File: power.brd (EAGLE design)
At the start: 65 x 80 mm, 19 parts, among them J1 Battery, J2 Solar, J3 Battery

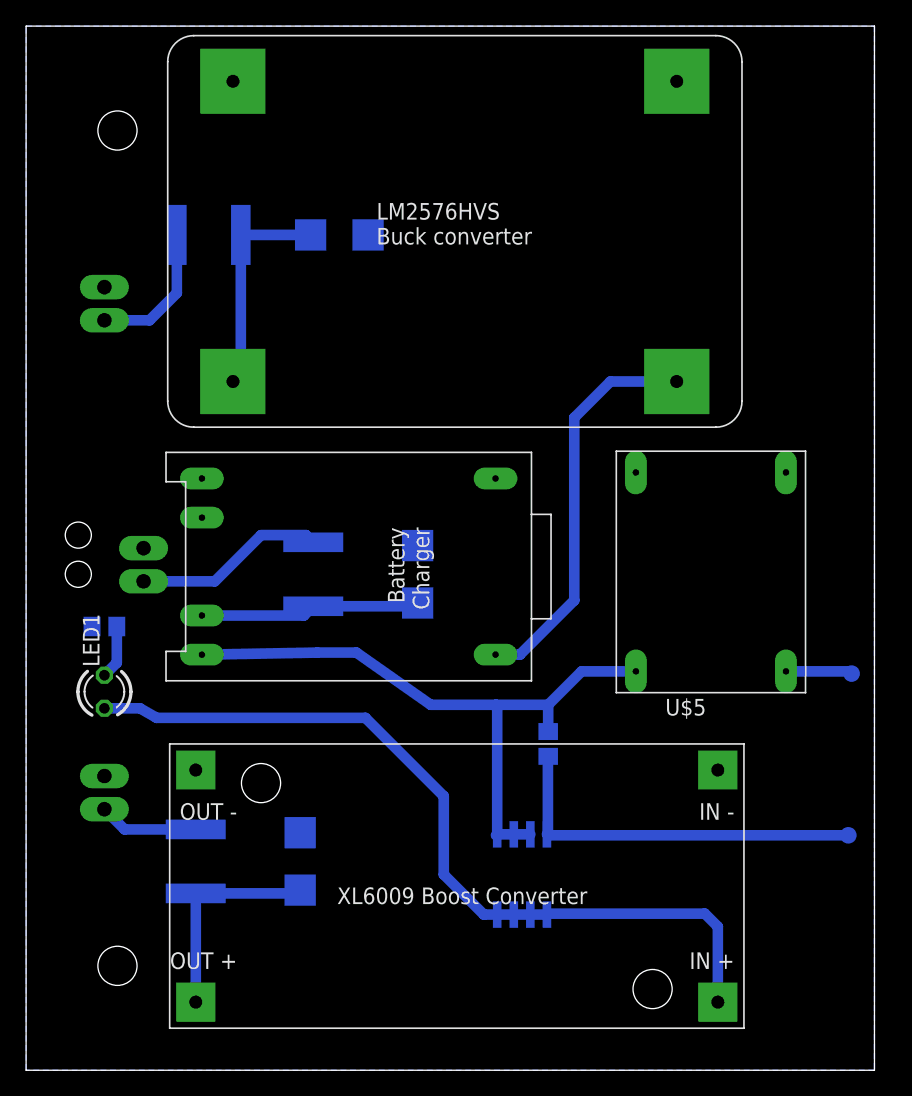
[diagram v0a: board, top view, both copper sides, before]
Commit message: Reworked power board
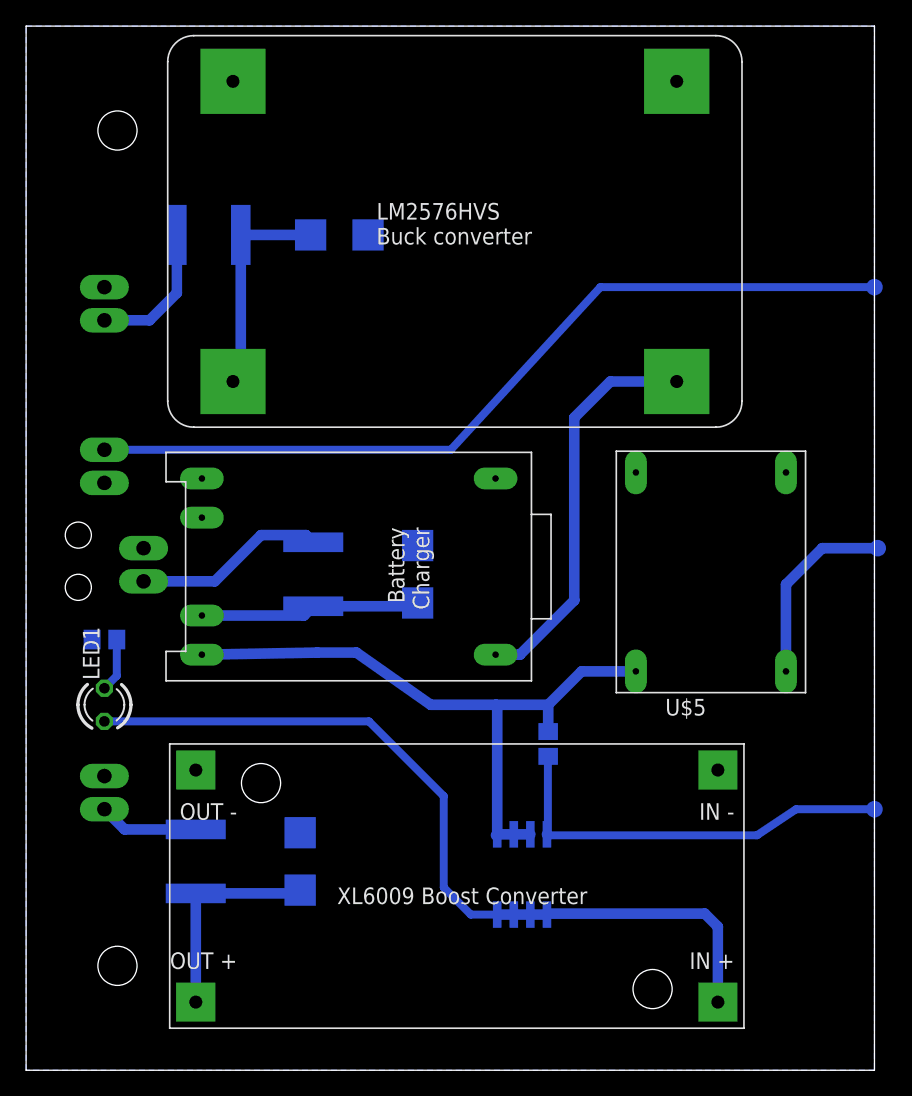
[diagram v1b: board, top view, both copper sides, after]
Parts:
- added J4: Button, SparkFun-Connectors:1X02_LONGPADS
- added TP1: TPSB1,27, testpad:B1,27
- J3: value Battery -> Valve
- U$3: value 2A -> 1A
- moved TP3 9.82 mm to (65.2, 40.0)
- moved TP5 2.83 mm to (65.0, 20.0)
- moved LED1 1.00 mm to (6.00, 28.0)
- moved R3 1.00 mm to (6.00, 33.0)
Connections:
- new net BUTTON_WAKEUP_INT: J4.2, TP1.TP
- net GND: now also J4.1
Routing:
- net BUTTON_WAKEUP_INT: track 0.00 -> 64.5 mm
- net VCC5: track 5.10 -> 14.8 mm
- net BT_POWER_ENABLE: track 29.2 -> 31.8 mm
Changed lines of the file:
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@@
 <hole x="7" y="8" drill="3"/>
 <hole x="4" y="41" drill="2"/>
-<hole x="4" y="38" drill="2"/>
+<hole x="4" y="37" drill="2"/>
 </plain>
 <attributes>
@@
 <element name="J1" library="SparkFun-Connectors" package="1X02_LONGPADS" value="Battery" x="9" y="40" rot="R270"/>
 <element name="J2" library="SparkFun-Connectors" package="1X02_LONGPADS" value="Solar" x="6" y="60" rot="R270"/>
-<element name="TP3" library="testpad" library_urn="urn:adsk.eagle:library:385" package="B1,27" package3d_urn="urn:adsk.eagle:package:27944/1" value="TPSB1,27" x="63.25" y="30.39" rot="MR0">
-<attribute name="TP_SIGNAL_NAME" value="" x="63.25" y="30.39" size="1.778" layer="28" rot="MR0" display="off"/>
+<element name="TP3" library="testpad" library_urn="urn:adsk.eagle:library:385" package="B1,27" package3d_urn="urn:adsk.eagle:package:27944/1" value="TPSB1,27" x="65.25" y="40" rot="MR0">
+<attribute name="TP_SIGNAL_NAME" value="" x="65.25" y="40" size="1.778" layer="28" rot="MR0" display="off"/>
 </element>
 <element name="U$10" library="fuse" library_urn="urn:adsk.eagle:library:233" package="MF-SMDF050" package3d_urn="urn:adsk.eagle:package:14081/1" value="500mA" x="14" y="64" rot="MR180"/>
@@
 <element name="U$5" library="breakout-modules" package="QSKJ_BOOST_MODULE" value="QSKJ_BOOST_MODULE" x="52.47" y="38.18"/>
 <element name="U$8" library="breakout-modules" package="LM2576HVS_BUCK_MODULE" value="LM2576HVS_BUCK_MODULE" x="10.85" y="49.27"/>
-<element name="LED1" library="led" library_urn="urn:adsk.eagle:library:259" package="LED3MM" package3d_urn="urn:adsk.eagle:package:15797/1" value="GREEN" x="6" y="29" rot="R90"/>
-<element name="R3" library="resistor" library_urn="urn:adsk.eagle:library:348" package="R0805" package3d_urn="urn:adsk.eagle:package:26059/1" value="3K3" x="6" y="34" rot="MR0"/>
+<element name="LED1" library="led" library_urn="urn:adsk.eagle:library:259" package="LED3MM" package3d_urn="urn:adsk.eagle:package:15797/1" value="GREEN" x="6" y="28" rot="R90"/>
+<element name="R3" library="resistor" library_urn="urn:adsk.eagle:library:348" package="R0805" package3d_urn="urn:adsk.eagle:package:26059/1" value="3K3" x="6" y="33" rot="MR0"/>
 <element name="R1" library="resistor" library_urn="urn:adsk.eagle:library:348" package="R0805" package3d_urn="urn:adsk.eagle:package:26059/1" value="1M" x="40" y="25" rot="MR270"/>
 <element name="U$6" library="breakout-modules" package="XL6009_BOOST_MODULE" value="XL6009_BOOST_MODULE" x="53" y="23" rot="R180"/>
 <element name="U$9" library="Semiconductors" package="SO08" value="FDS6675" x="38" y="15" rot="MR180"/>
-<element name="U$3" library="fuse" library_urn="urn:adsk.eagle:library:233" package="MF-SMDF050" package3d_urn="urn:adsk.eagle:package:14081/1" value="2A" x="13" y="16" rot="MR90"/>
+<element name="U$3" library="fuse" library_urn="urn:adsk.eagle:library:233" package="MF-SMDF050" package3d_urn="urn:adsk.eagle:package:14081/1" value="1A" x="13" y="16" rot="MR90"/>
 <element name="D4" library="diode" library_urn="urn:adsk.eagle:library:210" package="SMB" package3d_urn="urn:adsk.eagle:package:43404/2" value="" x="21" y="16" rot="MR90"/>
-<element name="J3" library="SparkFun-Connectors" package="1X02_LONGPADS" value="Battery" x="6" y="20" rot="R90"/>
-<element name="TP5" library="testpad" library_urn="urn:adsk.eagle:library:385" package="B1,27" package3d_urn="urn:adsk.eagle:package:27944/1" value="TPSB1,27" x="63" y="18" rot="MR0">
-<attribute name="TP_SIGNAL_NAME" value="" x="63" y="18" size="1.778" layer="28" rot="MR0" display="off"/>
+<element name="J3" library="SparkFun-Connectors" package="1X02_LONGPADS" value="Valve" x="6" y="20" rot="R90"/>
+<element name="TP5" library="testpad" library_urn="urn:adsk.eagle:library:385" package="B1,27" package3d_urn="urn:adsk.eagle:package:27944/1" value="TPSB1,27" x="65" y="20" rot="MR0">
+<attribute name="TP_SIGNAL_NAME" value="" x="65" y="20" size="1.778" layer="28" rot="MR0" display="off"/>
+</element>
+<element name="J4" library="SparkFun-Connectors" package="1X02_LONGPADS" value="Button" x="6" y="45" rot="R90"/>
+<element name="TP1" library="testpad" library_urn="urn:adsk.eagle:library:385" package="B1,27" package3d_urn="urn:adsk.eagle:package:27944/1" value="TPSB1,27" x="65" y="60" rot="MR90">
+<attribute name="TP_SIGNAL_NAME" value="" x="65" y="60" size="1.778" layer="28" rot="MR90" display="off"/>
 </element>
 </elements>
@@
 <contactref element="D4" pad="A"/>
 <contactref element="J3" pad="2"/>
+<contactref element="J4" pad="1"/>
 </signal>
 <signal name="VCC5">
 <contactref element="U$5" pad="V_OUT"/>
 <contactref element="TP3" pad="TP"/>
-<wire x1="58.22" y1="30.56" x2="63.08" y2="30.56" width="0.8128" layer="16"/>
-<wire x1="63.08" y1="30.56" x2="63.25" y2="30.39" width="0.8128" layer="16"/>
+<wire x1="58.22" y1="30.56" x2="58.22" y2="37.22" width="0.8128" layer="16"/>
+<wire x1="58.22" y1="37.22" x2="61" y2="40" width="0.8128" layer="16"/>
+<wire x1="61" y1="40" x2="65.25" y2="40" width="0.8128" layer="16"/>
 </signal>
 <signal name="V_CHARGER">
@@
 <contactref element="R3" pad="1"/>
 <contactref element="LED1" pad="K"/>
-<wire x1="6.95" y1="34" x2="6.95" y2="31.22" width="0.8128" layer="16"/>
-<wire x1="6.95" y1="31.22" x2="6" y2="30.27" width="0.8128" layer="16"/>
+<wire x1="6" y1="29.27" x2="6.95" y2="30.22" width="0.6096" layer="16"/>
+<wire x1="6.95" y1="30.22" x2="6.95" y2="33" width="0.6096" layer="16"/>
 </signal>
 <signal name="BT_POWER_ENABLE">
@@
 <contactref element="TP5" pad="TP"/>
 <wire x1="39.905" y1="18.0734" x2="39.9784" y2="18" width="0.8128" layer="16"/>
-<wire x1="39.9784" y1="18" x2="63" y2="18" width="0.8128" layer="16"/>
+<wire x1="39.9784" y1="18" x2="56" y2="18" width="0.6096" layer="16"/>
+<wire x1="56" y1="18" x2="59" y2="20" width="0.6096" layer="16"/>
+<wire x1="59" y1="20" x2="65" y2="20" width="0.6096" layer="16"/>
 <wire x1="40" y1="24.05" x2="39.9784" y2="24.0284" width="0.8128" layer="16"/>
-<wire x1="39.9784" y1="24.0284" x2="39.9784" y2="18" width="0.8128" layer="16"/>
+<wire x1="39.9784" y1="24.0284" x2="39.9784" y2="18" width="0.6096" layer="16"/>
 </signal>
 <signal name="V_VALVE_UNREG">
@@
 <wire x1="39.905" y1="11.9266" x2="39.9784" y2="12" width="0.8128" layer="16"/>
 <wire x1="39.9784" y1="12" x2="52" y2="12" width="0.8128" layer="16"/>
-<wire x1="26" y1="27" x2="10" y2="27" width="0.8128" layer="16"/>
-<wire x1="26" y1="27" x2="32" y2="21" width="0.8128" layer="16"/>
-<wire x1="32" y1="21" x2="32" y2="15" width="0.8128" layer="16"/>
-<wire x1="32" y1="15" x2="35.0734" y2="11.9266" width="0.8128" layer="16"/>
-<wire x1="35.0734" y1="11.9266" x2="36.095" y2="11.9266" width="0.8128" layer="16"/>
-<wire x1="10" y1="27" x2="8.73" y2="27.73" width="0.8128" layer="16"/>
-<wire x1="8.73" y1="27.73" x2="6" y2="27.73" width="0.8128" layer="16"/>
+<wire x1="6" y1="26.73" x2="26.27" y2="26.73" width="0.6096" layer="16"/>
+<wire x1="26.27" y1="26.73" x2="32" y2="21" width="0.6096" layer="16"/>
+<wire x1="32" y1="21" x2="32" y2="14" width="0.6096" layer="16"/>
+<wire x1="32" y1="14" x2="34.0734" y2="11.9266" width="0.6096" layer="16"/>
+<wire x1="34.0734" y1="11.9266" x2="36.095" y2="11.9266" width="0.6096" layer="16"/>
 </signal>
 <signal name="VALVE">
@@
 <wire x1="20.75" y1="13.55" x2="21" y2="13.8" width="0.8128" layer="16"/>
 </signal>
+<signal name="BUTTON_WAKEUP_INT">
+<contactref element="TP1" pad="TP"/>
+<contactref element="J4" pad="2"/>
+<wire x1="6" y1="47.54" x2="32.54" y2="47.54" width="0.6096" layer="16"/>
+<wire x1="32.54" y1="47.54" x2="44" y2="60" width="0.6096" layer="16"/>
+<wire x1="44" y1="60" x2="65" y2="60" width="0.6096" layer="16"/>
+</signal>
 </signals>

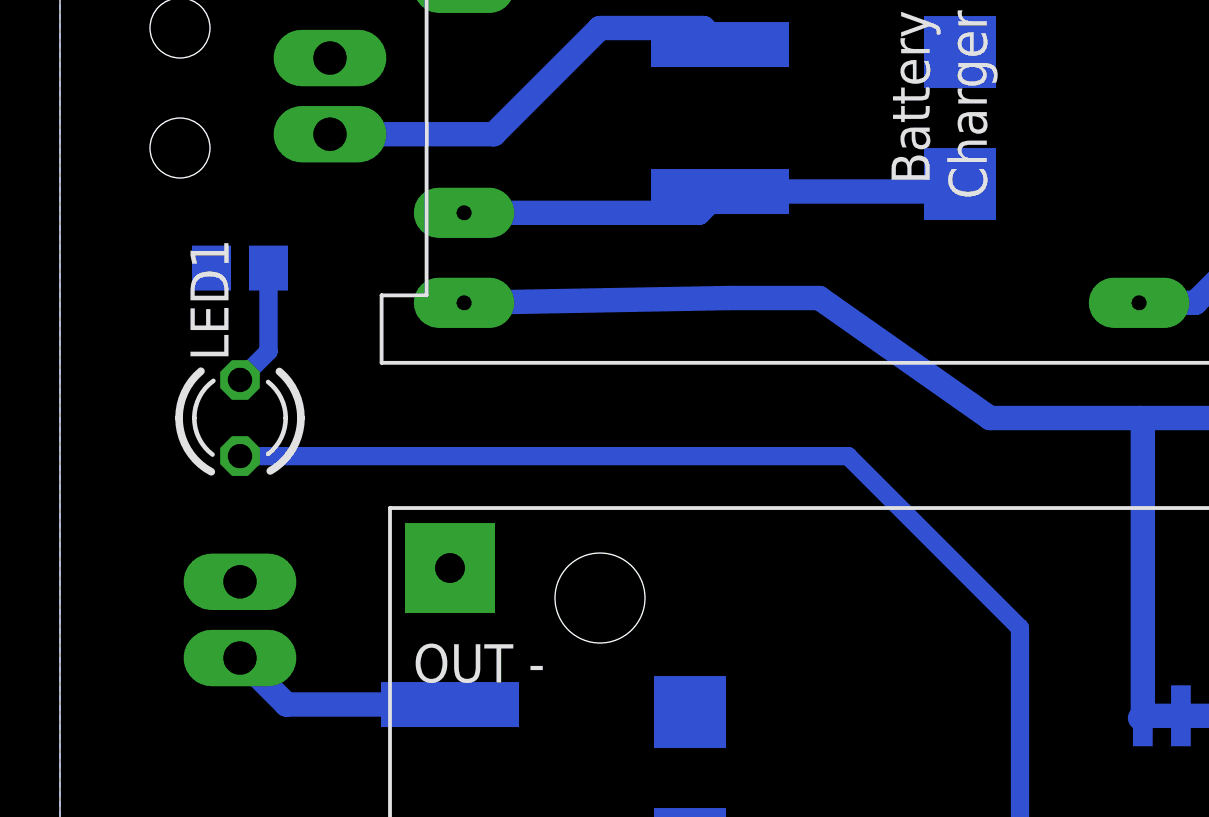
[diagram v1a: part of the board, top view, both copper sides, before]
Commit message: Fill to edge
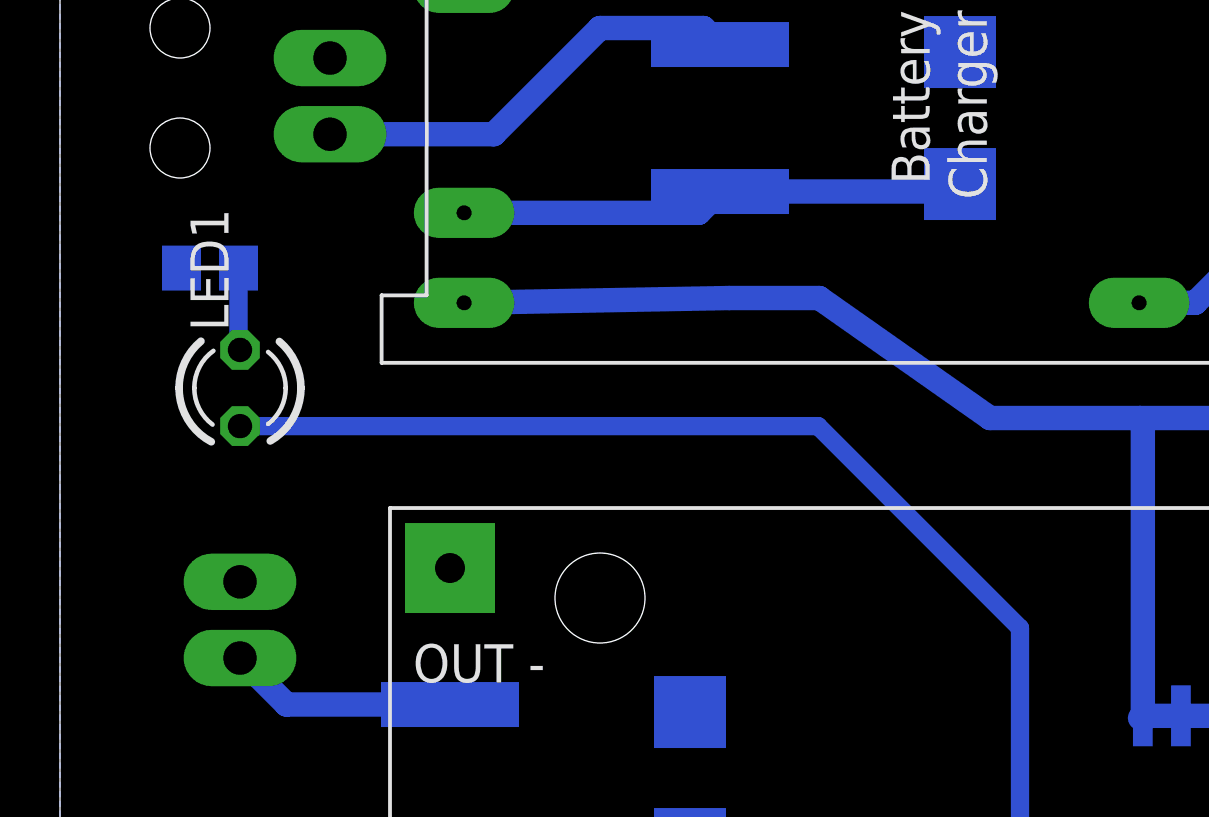
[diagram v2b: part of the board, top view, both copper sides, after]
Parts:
- moved LED1 1.00 mm to (6.00, 29.0)
- moved R3 1.00 mm to (5.00, 33.0)
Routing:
- net N$9: track 4.12 -> 2.85 mm
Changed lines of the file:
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@@
 </class>
 </classes>
-<designrules name="default">
+<designrules name="default *">
 <description language="de">&lt;b&gt;EAGLE Design Rules&lt;/b&gt;
 &lt;p&gt;
@@
 <param name="mdViaViaSameLayer" value="6mil"/>
 <param name="mnLayersViaInSmd" value="2"/>
-<param name="mdCopperDimension" value="40mil"/>
+<param name="mdCopperDimension" value="0mil"/>
 <param name="mdDrill" value="6mil"/>
 <param name="mdSmdStop" value="0mil"/>
@@
 <element name="U$5" library="breakout-modules" package="QSKJ_BOOST_MODULE" value="QSKJ_BOOST_MODULE" x="52.47" y="38.18"/>
 <element name="U$8" library="breakout-modules" package="LM2576HVS_BUCK_MODULE" value="LM2576HVS_BUCK_MODULE" x="10.85" y="49.27"/>
-<element name="LED1" library="led" library_urn="urn:adsk.eagle:library:259" package="LED3MM" package3d_urn="urn:adsk.eagle:package:15797/1" value="GREEN" x="6" y="28" rot="R90"/>
-<element name="R3" library="resistor" library_urn="urn:adsk.eagle:library:348" package="R0805" package3d_urn="urn:adsk.eagle:package:26059/1" value="3K3" x="6" y="33" rot="MR0"/>
+<element name="LED1" library="led" library_urn="urn:adsk.eagle:library:259" package="LED3MM" package3d_urn="urn:adsk.eagle:package:15797/1" value="GREEN" x="6" y="29" rot="R90"/>
+<element name="R3" library="resistor" library_urn="urn:adsk.eagle:library:348" package="R0805" package3d_urn="urn:adsk.eagle:package:26059/1" value="3K3" x="5" y="33" rot="MR0"/>
 <element name="R1" library="resistor" library_urn="urn:adsk.eagle:library:348" package="R0805" package3d_urn="urn:adsk.eagle:package:26059/1" value="1M" x="40" y="25" rot="MR270"/>
 <element name="U$6" library="breakout-modules" package="XL6009_BOOST_MODULE" value="XL6009_BOOST_MODULE" x="53" y="23" rot="R180"/>
@@
 <contactref element="J2" pad="1"/>
 <contactref element="J1" pad="1"/>
-<polygon width="0.8128" layer="16" isolate="1.016">
+<polygon width="0" layer="16" isolate="1.016">
 <vertex x="0" y="80"/>
 <vertex x="65" y="80"/>
@@
 <contactref element="R3" pad="1"/>
 <contactref element="LED1" pad="K"/>
-<wire x1="6" y1="29.27" x2="6.95" y2="30.22" width="0.6096" layer="16"/>
-<wire x1="6.95" y1="30.22" x2="6.95" y2="33" width="0.6096" layer="16"/>
+<wire x1="6" y1="30.27" x2="5.95" y2="30.22" width="0.6096" layer="16"/>
+<wire x1="5.95" y1="30.22" x2="5.95" y2="33" width="0.6096" layer="16"/>
 </signal>
 <signal name="BT_POWER_ENABLE">
@@
 <wire x1="39.905" y1="11.9266" x2="39.9784" y2="12" width="0.8128" layer="16"/>
 <wire x1="39.9784" y1="12" x2="52" y2="12" width="0.8128" layer="16"/>
-<wire x1="6" y1="26.73" x2="26.27" y2="26.73" width="0.6096" layer="16"/>
-<wire x1="26.27" y1="26.73" x2="32" y2="21" width="0.6096" layer="16"/>
+<wire x1="6" y1="27.73" x2="25.27" y2="27.73" width="0.6096" layer="16"/>
+<wire x1="25.27" y1="27.73" x2="32" y2="21" width="0.6096" layer="16"/>
 <wire x1="32" y1="21" x2="32" y2="14" width="0.6096" layer="16"/>
 <wire x1="32" y1="14" x2="34.0734" y2="11.9266" width="0.6096" layer="16"/>
